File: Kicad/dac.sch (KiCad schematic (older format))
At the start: 13 parts

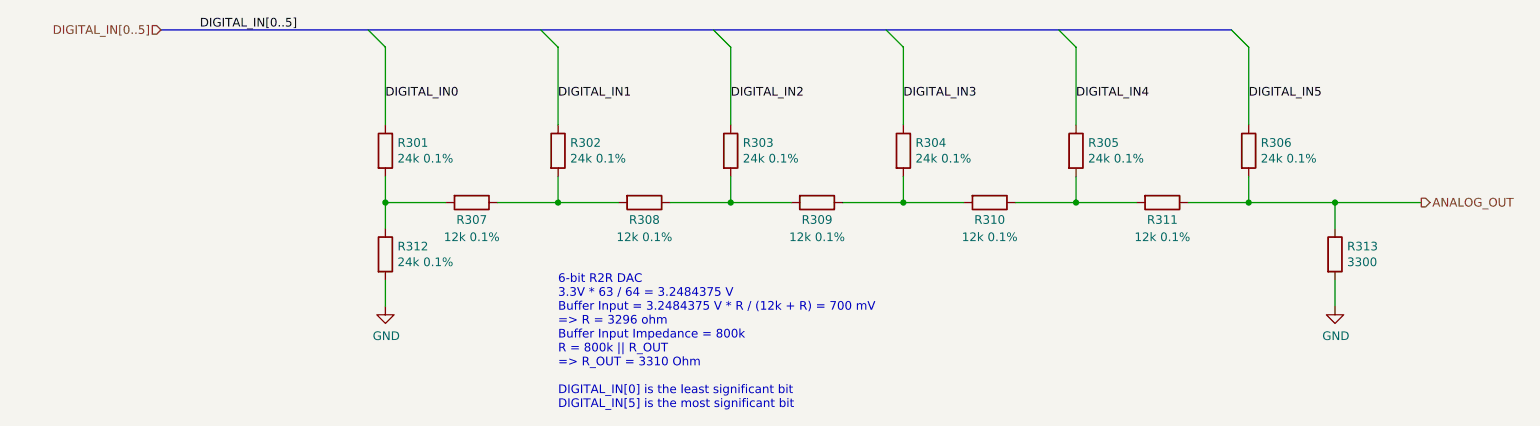
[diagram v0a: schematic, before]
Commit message: Replaced KE04Z with STM32F0.
Had trouble debugging a test KE06Z device. Decided an STM32 would be simpler.
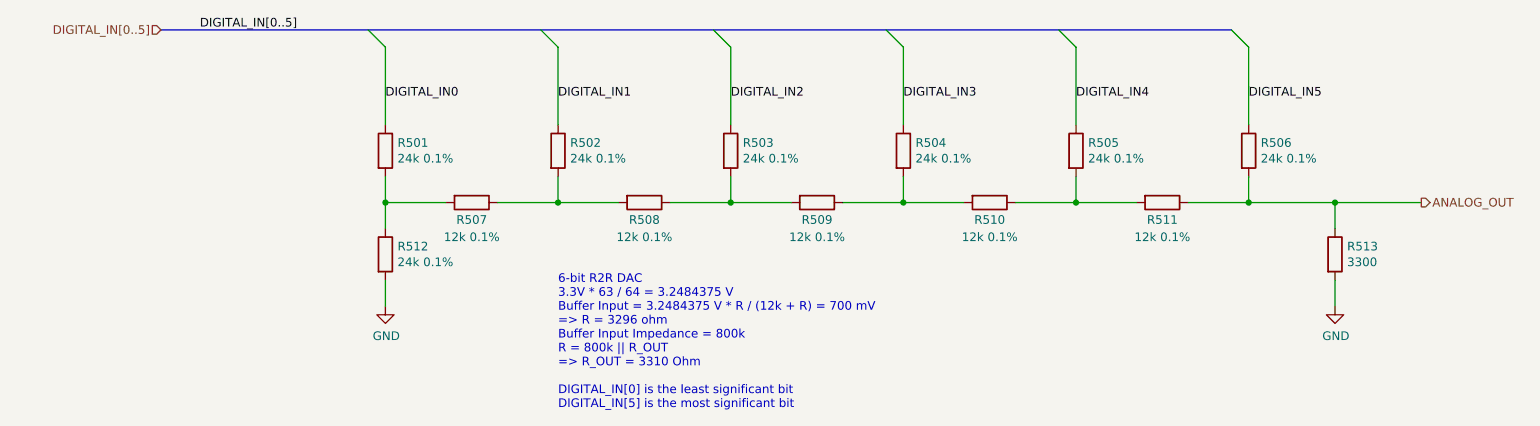
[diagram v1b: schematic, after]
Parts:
- R301, R302, R303, R304, R305, R306, R307, R308, R309, R310, R311, R312, R313: DNP (none) -> 0
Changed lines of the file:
@@
 AR Path="/5FDE658D/6009CBAC/5F5F4D05" Ref="R401"  Part="1"
 AR Path="/5FDE658D/600A04B7/5F5F4D05" Ref="R501"  Part="1"
-F 0 "R301" H 3570 2746 50  0000 L CNN
+F 0 "R501" H 3570 2746 50  0000 L CNN
 F 1 "24k 0.1%" H 3570 2655 50  0000 L CNN
 F 2 "Resistor_SMD:R_0805_2012Metric_Pad1.15x1.40mm_HandSolder" V 3430 2700 50  0001 C CNN
 F 3 "~" H 3500 2700 50  0001 C CNN
+F 4 "0" H 3500 2700 50  0001 C CNN "DNP"
 	1    3500 2700
 	1    0    0    -1
@@
 AR Path="/5FDE658D/6009CBAC/5F5F5C61" Ref="R407"  Part="1"
 AR Path="/5FDE658D/600A04B7/5F5F5C61" Ref="R507"  Part="1"
-F 0 "R307" V 4100 3000 50  0000 C CNN
+F 0 "R507" V 4100 3000 50  0000 C CNN
 F 1 "12k 0.1%" V 4200 3000 50  0000 C CNN
 F 2 "Resistor_SMD:R_0805_2012Metric_Pad1.15x1.40mm_HandSolder" V 3930 3000 50  0001 C CNN
 F 3 "~" H 4000 3000 50  0001 C CNN
+F 4 "0" H 4000 3000 50  0001 C CNN "DNP"
 	1    4000 3000
 	0    1    1    0
@@
 AR Path="/5FDE658D/6009CBAC/5F5F6568" Ref="R402"  Part="1"
 AR Path="/5FDE658D/600A04B7/5F5F6568" Ref="R502"  Part="1"
-F 0 "R302" H 4570 2746 50  0000 L CNN
+F 0 "R502" H 4570 2746 50  0000 L CNN
 F 1 "24k 0.1%" H 4570 2655 50  0000 L CNN
 F 2 "Resistor_SMD:R_0805_2012Metric_Pad1.15x1.40mm_HandSolder" V 4430 2700 50  0001 C CNN
 F 3 "~" H 4500 2700 50  0001 C CNN
+F 4 "0" H 4500 2700 50  0001 C CNN "DNP"
 	1    4500 2700
 	1    0    0    -1
@@
 AR Path="/5FDE658D/6009CBAC/5F5F6D42" Ref="R408"  Part="1"
 AR Path="/5FDE658D/600A04B7/5F5F6D42" Ref="R508"  Part="1"
-F 0 "R308" V 5100 3000 50  0000 C CNN
+F 0 "R508" V 5100 3000 50  0000 C CNN
 F 1 "12k 0.1%" V 5200 3000 50  0000 C CNN
 F 2 "Resistor_SMD:R_0805_2012Metric_Pad1.15x1.40mm_HandSolder" V 4930 3000 50  0001 C CNN
 F 3 "~" H 5000 3000 50  0001 C CNN
+F 4 "0" H 5000 3000 50  0001 C CNN "DNP"
 	1    5000 3000
 	0    1    1    0
@@
 AR Path="/5FDE658D/6009CBAC/5F5F6F45" Ref="R409"  Part="1"
 AR Path="/5FDE658D/600A04B7/5F5F6F45" Ref="R509"  Part="1"
-F 0 "R309" V 6100 3000 50  0000 C CNN
+F 0 "R509" V 6100 3000 50  0000 C CNN
 F 1 "12k 0.1%" V 6200 3000 50  0000 C CNN
 F 2 "Resistor_SMD:R_0805_2012Metric_Pad1.15x1.40mm_HandSolder" V 5930 3000 50  0001 C CNN
 F 3 "~" H 6000 3000 50  0001 C CNN
+F 4 "0" H 6000 3000 50  0001 C CNN "DNP"
 	1    6000 3000
 	0    1    1    0
@@
 AR Path="/5FDE658D/6009CBAC/5F5F984D" Ref="R410"  Part="1"
 AR Path="/5FDE658D/600A04B7/5F5F984D" Ref="R510"  Part="1"
-F 0 "R310" V 7100 3000 50  0000 C CNN
+F 0 "R510" V 7100 3000 50  0000 C CNN
 F 1 "12k 0.1%" V 7200 3000 50  0000 C CNN
 F 2 "Resistor_SMD:R_0805_2012Metric_Pad1.15x1.40mm_HandSolder" V 6930 3000 50  0001 C CNN
 F 3 "~" H 7000 3000 50  0001 C CNN
+F 4 "0" H 7000 3000 50  0001 C CNN "DNP"
 	1    7000 3000
 	0    1    1    0
@@
 AR Path="/5FDE658D/6009CBAC/5F5F99D6" Ref="R411"  Part="1"
 AR Path="/5FDE658D/600A04B7/5F5F99D6" Ref="R511"  Part="1"
-F 0 "R311" V 8100 3000 50  0000 C CNN
+F 0 "R511" V 8100 3000 50  0000 C CNN
 F 1 "12k 0.1%" V 8200 3000 50  0000 C CNN
 F 2 "Resistor_SMD:R_0805_2012Metric_Pad1.15x1.40mm_HandSolder" V 7930 3000 50  0001 C CNN
 F 3 "~" H 8000 3000 50  0001 C CNN
+F 4 "0" H 8000 3000 50  0001 C CNN "DNP"
 	1    8000 3000
 	0    1    1    0
@@
 AR Path="/5FDE658D/6009CBAC/5F5FA2EE" Ref="R413"  Part="1"
 AR Path="/5FDE658D/600A04B7/5F5FA2EE" Ref="R513"  Part="1"
-F 0 "R313" H 9070 3346 50  0000 L CNN
+F 0 "R513" H 9070 3346 50  0000 L CNN
 F 1 "3300" H 9070 3255 50  0000 L CNN
 F 2 "Resistor_SMD:R_0805_2012Metric_Pad1.15x1.40mm_HandSolder" V 8930 3300 50  0001 C CNN
 F 3 "~" H 9000 3300 50  0001 C CNN
+F 4 "0" H 9000 3300 50  0001 C CNN "DNP"
 	1    9000 3300
 	1    0    0    -1
@@
 AR Path="/5FDE658D/6009CBAC/5F5FBB89" Ref="#PWR0401"  Part="1"
 AR Path="/5FDE658D/600A04B7/5F5FBB89" Ref="#PWR0501"  Part="1"
-F 0 "#PWR0301" H 3500 3350 50  0001 C CNN
+F 0 "#PWR0501" H 3500 3350 50  0001 C CNN
 F 1 "GND" H 3505 3427 50  0000 C CNN
 F 2 "" H 3500 3600 50  0001 C CNN
@@
 AR Path="/5FDE658D/6009CBAC/5F5FBF42" Ref="#PWR0402"  Part="1"
 AR Path="/5FDE658D/600A04B7/5F5FBF42" Ref="#PWR0502"  Part="1"
-F 0 "#PWR0302" H 9000 3350 50  0001 C CNN
+F 0 "#PWR0502" H 9000 3350 50  0001 C CNN
 F 1 "GND" H 9005 3427 50  0000 C CNN
 F 2 "" H 9000 3600 50  0001 C CNN
@@
 AR Path="/5FDE658D/6009CBAC/5F5FCF8C" Ref="R412"  Part="1"
 AR Path="/5FDE658D/600A04B7/5F5FCF8C" Ref="R512"  Part="1"
-F 0 "R312" H 3570 3346 50  0000 L CNN
+F 0 "R512" H 3570 3346 50  0000 L CNN
 F 1 "24k 0.1%" H 3570 3255 50  0000 L CNN
 F 2 "Resistor_SMD:R_0805_2012Metric_Pad1.15x1.40mm_HandSolder" V 3430 3300 50  0001 C CNN
 F 3 "~" H 3500 3300 50  0001 C CNN
+F 4 "0" H 3500 3300 50  0001 C CNN "DNP"
 	1    3500 3300
 	1    0    0    -1
@@
 AR Path="/5FDE658D/6009CBAC/5F5FD13B" Ref="R403"  Part="1"
 AR Path="/5FDE658D/600A04B7/5F5FD13B" Ref="R503"  Part="1"
-F 0 "R303" H 5570 2746 50  0000 L CNN
+F 0 "R503" H 5570 2746 50  0000 L CNN
 F 1 "24k 0.1%" H 5570 2655 50  0000 L CNN
 F 2 "Resistor_SMD:R_0805_2012Metric_Pad1.15x1.40mm_HandSolder" V 5430 2700 50  0001 C CNN
 F 3 "~" H 5500 2700 50  0001 C CNN
+F 4 "0" H 5500 2700 50  0001 C CNN "DNP"
 	1    5500 2700
 	1    0    0    -1
@@
 AR Path="/5FDE658D/6009CBAC/5F5FD329" Ref="R404"  Part="1"
 AR Path="/5FDE658D/600A04B7/5F5FD329" Ref="R504"  Part="1"
-F 0 "R304" H 6570 2746 50  0000 L CNN
+F 0 "R504" H 6570 2746 50  0000 L CNN
 F 1 "24k 0.1%" H 6570 2655 50  0000 L CNN
 F 2 "Resistor_SMD:R_0805_2012Metric_Pad1.15x1.40mm_HandSolder" V 6430 2700 50  0001 C CNN
 F 3 "~" H 6500 2700 50  0001 C CNN
+F 4 "0" H 6500 2700 50  0001 C CNN "DNP"
 	1    6500 2700
 	1    0    0    -1
@@
 AR Path="/5FDE658D/6009CBAC/5F5FD46F" Ref="R405"  Part="1"
 AR Path="/5FDE658D/600A04B7/5F5FD46F" Ref="R505"  Part="1"
-F 0 "R305" H 7570 2746 50  0000 L CNN
+F 0 "R505" H 7570 2746 50  0000 L CNN
 F 1 "24k 0.1%" H 7570 2655 50  0000 L CNN
 F 2 "Resistor_SMD:R_0805_2012Metric_Pad1.15x1.40mm_HandSolder" V 7430 2700 50  0001 C CNN
 F 3 "~" H 7500 2700 50  0001 C CNN
+F 4 "0" H 7500 2700 50  0001 C CNN "DNP"
 	1    7500 2700
 	1    0    0    -1
@@
 AR Path="/5FDE658D/6009CBAC/5F5FD6C1" Ref="R406"  Part="1"
 AR Path="/5FDE658D/600A04B7/5F5FD6C1" Ref="R506"  Part="1"
-F 0 "R306" H 8570 2746 50  0000 L CNN
+F 0 "R506" H 8570 2746 50  0000 L CNN
 F 1 "24k 0.1%" H 8570 2655 50  0000 L CNN
 F 2 "Resistor_SMD:R_0805_2012Metric_Pad1.15x1.40mm_HandSolder" V 8430 2700 50  0001 C CNN
 F 3 "~" H 8500 2700 50  0001 C CNN
+F 4 "0" H 8500 2700 50  0001 C CNN "DNP"
 	1    8500 2700
 	1    0    0    -1
